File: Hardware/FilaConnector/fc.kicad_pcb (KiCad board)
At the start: 2 copper layers, 27.9 x 15.2 mm, 5 parts, among them J1 Conn_1, J2 Conn_2, J3 PWR_IN, SW1 PowerSel

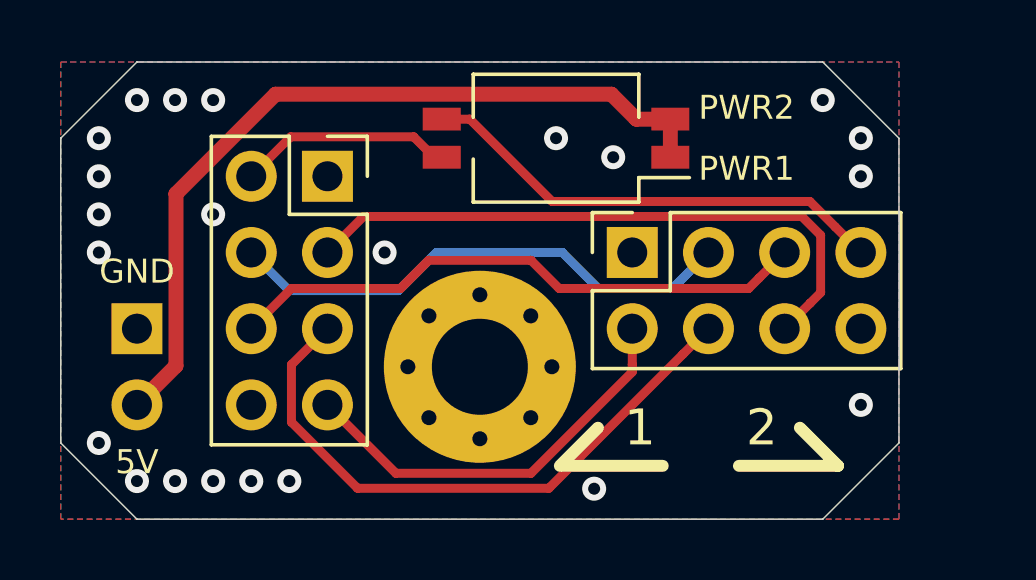
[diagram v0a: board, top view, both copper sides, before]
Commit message: updated wall cell and connector
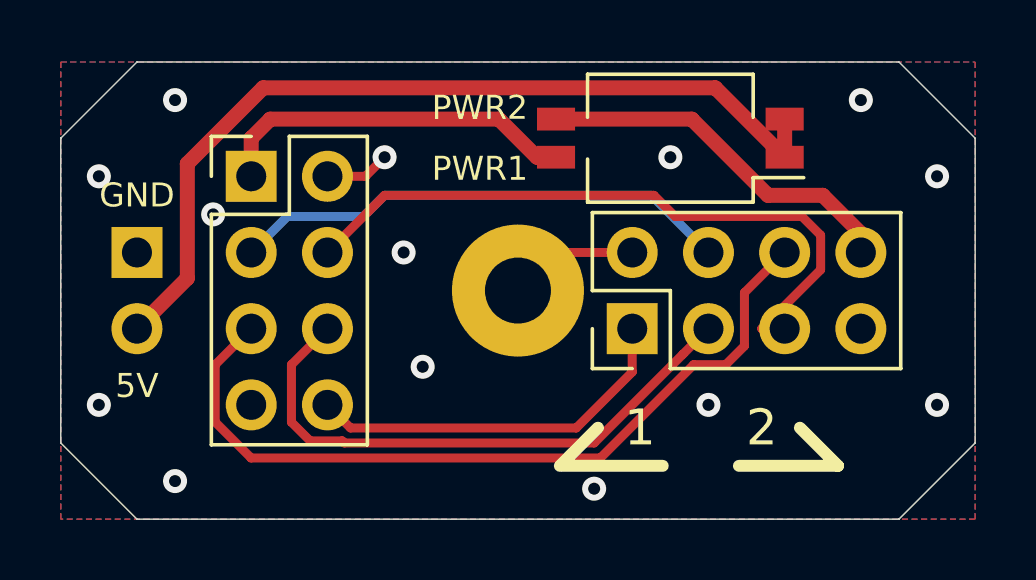
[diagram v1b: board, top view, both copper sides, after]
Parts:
- H1: footprint MountingHole:MountingHole_3.2mm_M3_Pad_Via -> MountingHole:MountingHole_2.2mm_M2_Pad
- J1, J2: footprint Connector_PinSocket_2.54mm:PinSocket_2x04_P2.54mm_Vertical -> Connector_PinHeader_2.54mm:PinHeader_2x04_P2.54mm_Vertical
- moved SW1 3.81 mm to (106.7, 43.2)
- moved H1 2.84 mm to (101.6, 48.3)
- moved J1 2.54 mm to (92.7, 44.5)
- moved J2 2.54 mm to (105.4, 49.5)
- moved J3 2.54 mm to (88.9, 47.0)
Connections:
- J1 pad 1: GND -> /5v_CON1
- J1 pad 2: /5v_CON1 -> GND
- J1 pad 3: CLK -> SD_2TO1
- J1 pad 4: SD_2TO1 -> CLK
- J1 pad 5: LE -> SD_1TO2
- J1 pad 6: SD_1TO2 -> LE
- J1 pad 7: OE -> GND
- J1 pad 8: GND -> OE
- J2 pad 1: GND -> OE
- J2 pad 2: OE -> GND
- J2 pad 3: SD_2TO1 -> LE
- J2 pad 4: LE -> SD_2TO1
- J2 pad 5: SD_1TO2 -> CLK
- J2 pad 6: CLK -> SD_1TO2
- J2 pad 7: /5v_CON2 -> GND
- J2 pad 8: GND -> /5v_CON2
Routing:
- net GND: track 0.00 -> 7.77 mm, vias 22 -> 14
- net SD_1TO2: track 19.6 -> 27.0 mm
- net /5v_CON1: track 7.18 -> 12.2 mm
- net /5v_CON2: track 15.8 -> 12.4 mm
- net /5v_PWR: track 27.0 -> 29.4 mm
- net CLK: track 20.8 -> 22.5 mm
- net LE: track 20.6 -> 19.4 mm
- net OE: track 13.9 -> 12.7 mm
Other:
- board size 27.9 x 15.2 mm -> 30.5 x 15.2 mm
- rule pad_to_mask_clearance: 0.051 -> 0
- board text added: "Fila Connector v0.2 Sandbox Workshop Designed by Caorx Wangyw"
- board text removed: "Fila Connector v0.1 Sandbox Workshop Designed by Caorx Wangyw"

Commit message: updated packages
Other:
- board text added: "Fila Connector v0.2 Sandbox Workshop 2021-04 Designed by Caorx Wangyw"
- board text removed: "Fila Connector v0.2 Sandbox Workshop Designed by Caorx Wangyw"

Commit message: merged all
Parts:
- removed H1: MountingHole_Pad, MountingHole:MountingHole_2.2mm_M2_Pad
- J1, J2: footprint Connector_PinHeader_2.54mm:PinHeader_2x04_P2.54mm_Vertical -> Connector_PinSocket_2.54mm:PinSocket_2x04_P2.54mm_Vertical
- moved J1 2.54 mm to (95.2, 44.5)
- moved J2 2.54 mm to (105.4, 47.0)
- moved SW1 2.54 mm to (109.2, 43.2), turned to 0 degrees
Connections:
- J1 pad 1: /5v_CON1 -> GND
- J1 pad 2: GND -> /5v_CON1
- J1 pad 3: SD_2TO1 -> CLK
- J1 pad 4: CLK -> SD_2TO1
- J1 pad 5: SD_1TO2 -> LE
- J1 pad 6: LE -> SD_1TO2
- J1 pad 7: GND -> OE
- J1 pad 8: OE -> GND
- J2 pad 1: OE -> GND
- J2 pad 2: GND -> OE
- J2 pad 3: LE -> SD_2TO1
- J2 pad 4: SD_2TO1 -> LE
- J2 pad 5: CLK -> SD_1TO2
- J2 pad 6: SD_1TO2 -> CLK
- J2 pad 7: GND -> /5v_CON2
- J2 pad 8: /5v_CON2 -> GND
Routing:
- net /5v_CON1: track 12.2 -> 22.7 mm
- net /5v_CON2: track 12.4 -> 3.18 mm
- net GND: track 7.77 -> 0.00 mm, vias 14 -> 9
- net /5v_PWR: track 29.4 -> 23.9 mm
- net CLK: track 22.5 -> 20.9 mm
- net OE: track 12.7 -> 11.2 mm
- net SD_2TO1: track 16.8 -> 16.2 mm
- net LE: track 19.4 -> 20.0 mm
- net SD_1TO2: track 27.0 -> 27.5 mm
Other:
- outline, holes or cut-outs redrawn
- board text added: "CLK"
- board text added: "D12"
- board text added: "D21"
- board text added: "Fila Connector v0.3 Sandbox 2021-04 By Caorx Wangyw"
- board text added: "JLCJLCJLCJLC"
- board text added: "LE"
- board text added: "OE"
- board text added: "P1"
- board text added: "P2"
- board text removed: "Fila Connector v0.2 Sandbox Workshop 2021-04 Designed by Caorx Wangyw"
- board text removed: "PWR1"
- board text removed: "PWR2"
